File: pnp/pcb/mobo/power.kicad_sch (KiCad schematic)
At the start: 31 parts, among them J12 COMBO_POWER_JACK, U11 FDS4435BZ, U12 TPS54331, U13 AP1117-33, U6 Fuse_Holder_3568

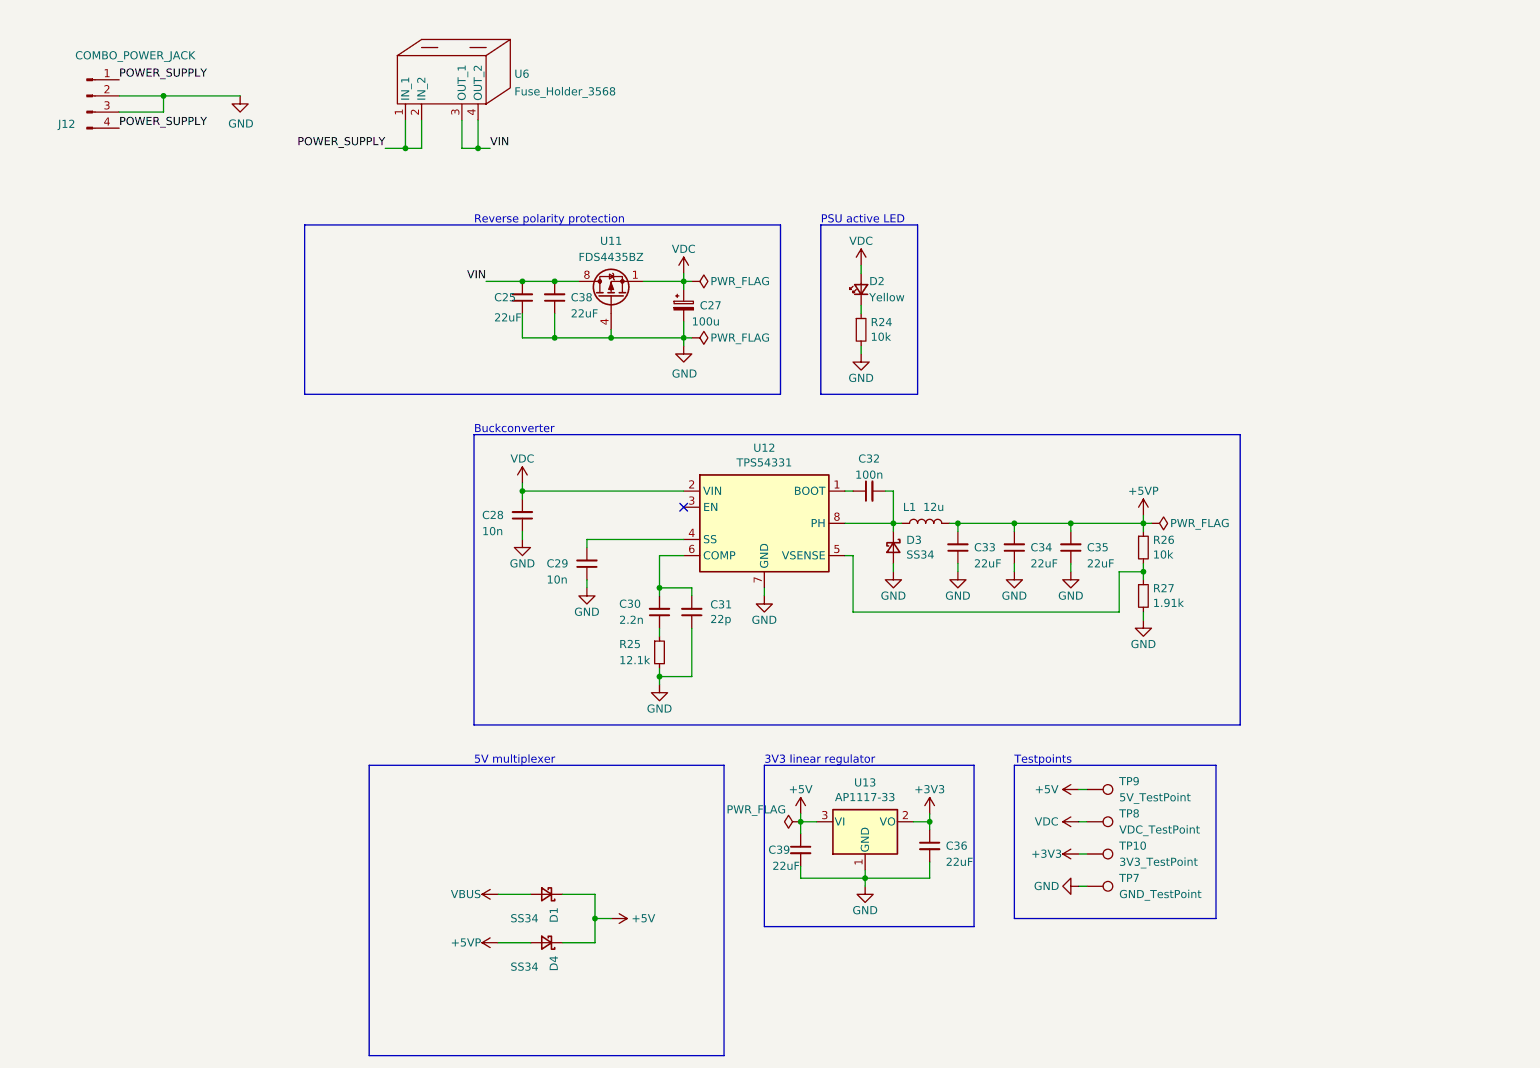
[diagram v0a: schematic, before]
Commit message: Mobo V4A Redesign
Some EMC improvements to schematics.
Reassigned MCU Pins for HW-PWM support.
Changes are still marked with text in the schematics.
Complete PCB Layout reworked
Status: Needs to be verified, and cleaned up a little, but DRC is running green.
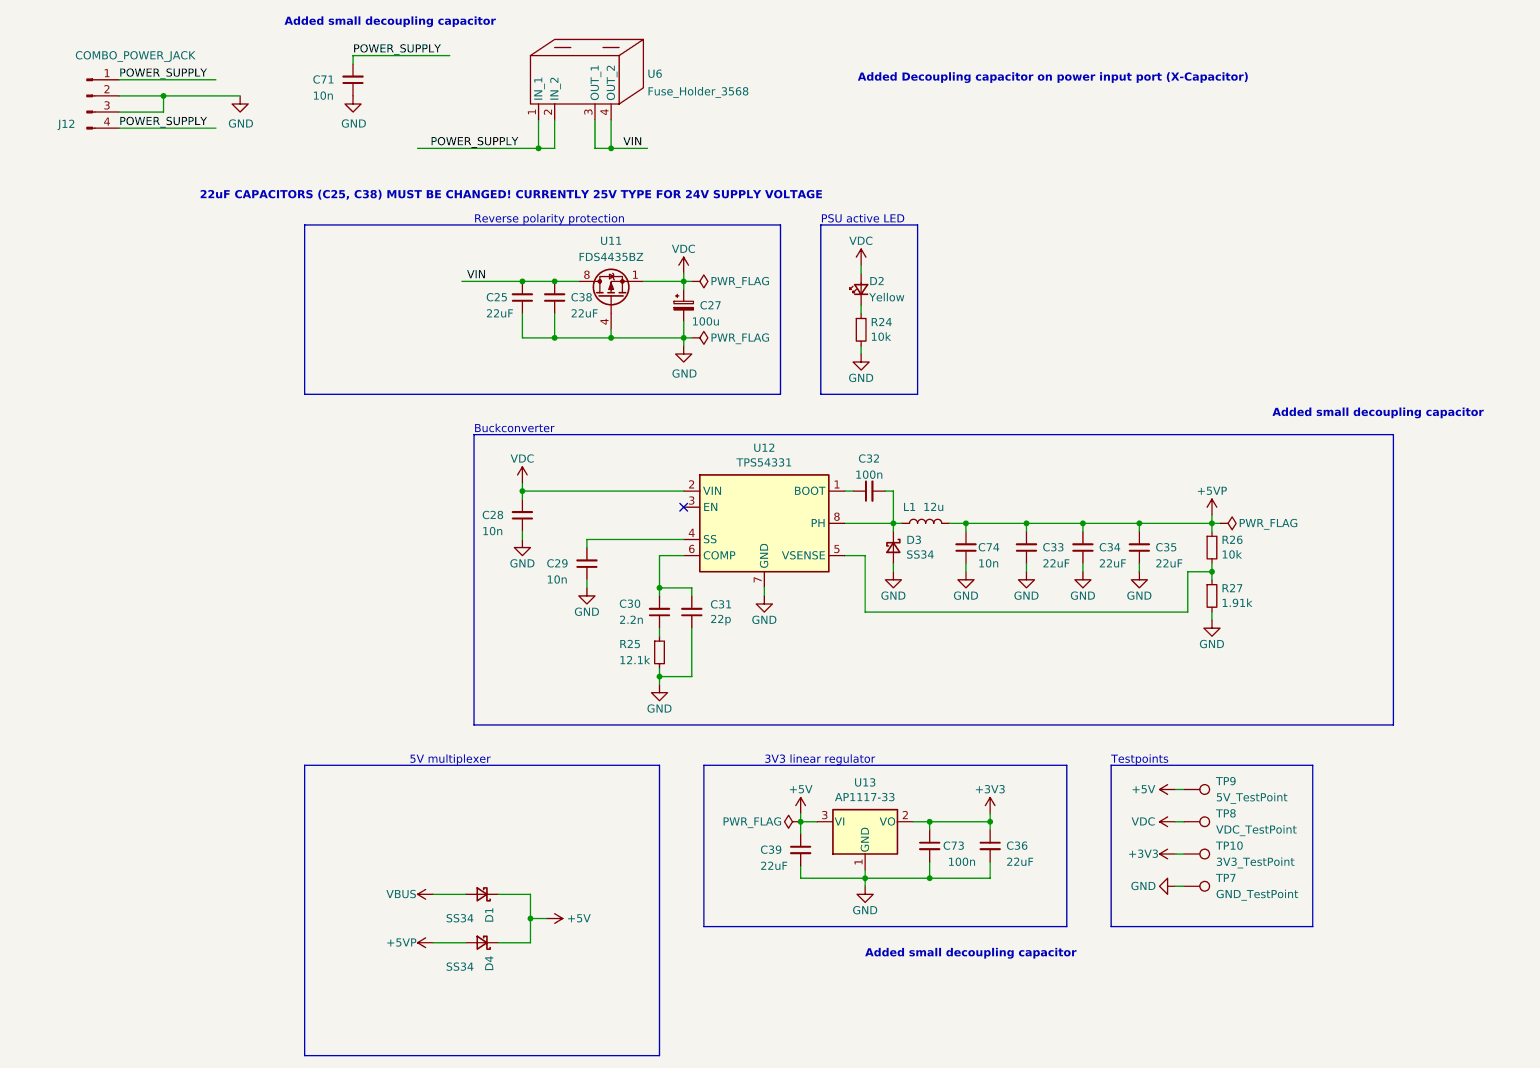
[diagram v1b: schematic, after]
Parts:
- added C71, C74: 10n, Capacitor_SMD:C_0805_2012Metric, symbol Device:C_Small
- added C73: 100n, Capacitor_SMD:C_0805_2012Metric, symbol Device:C_Small
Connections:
- net +3V3: now also C73.1
- net +5VP: now also C74.2
- net GND: now also C71.1, C73.2, C74.1
- net POWER_SUPPLY: now also C71.2
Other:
- note added: "22uF CAPACITORS (C25, C38) MUST BE CHANGED! CURRENTLY 25V TYPE FOR 24V SUPPLY VOLTAGE"
- note added: "Added Decoupling capacitor on power input port (X-Capacitor)"
- note added: "Added small decoupling capacitor"
- moved on the sheet: C33, C34, C35, C36, D1, D4, R26, R27, TP10, TP7, TP8, TP9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

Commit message: Redesign finished
Completed Board redesign and adding more EMC improvements.
Changed all the part numbers to have a Mouser orderable design (except the JST connectors)
All outputs generated
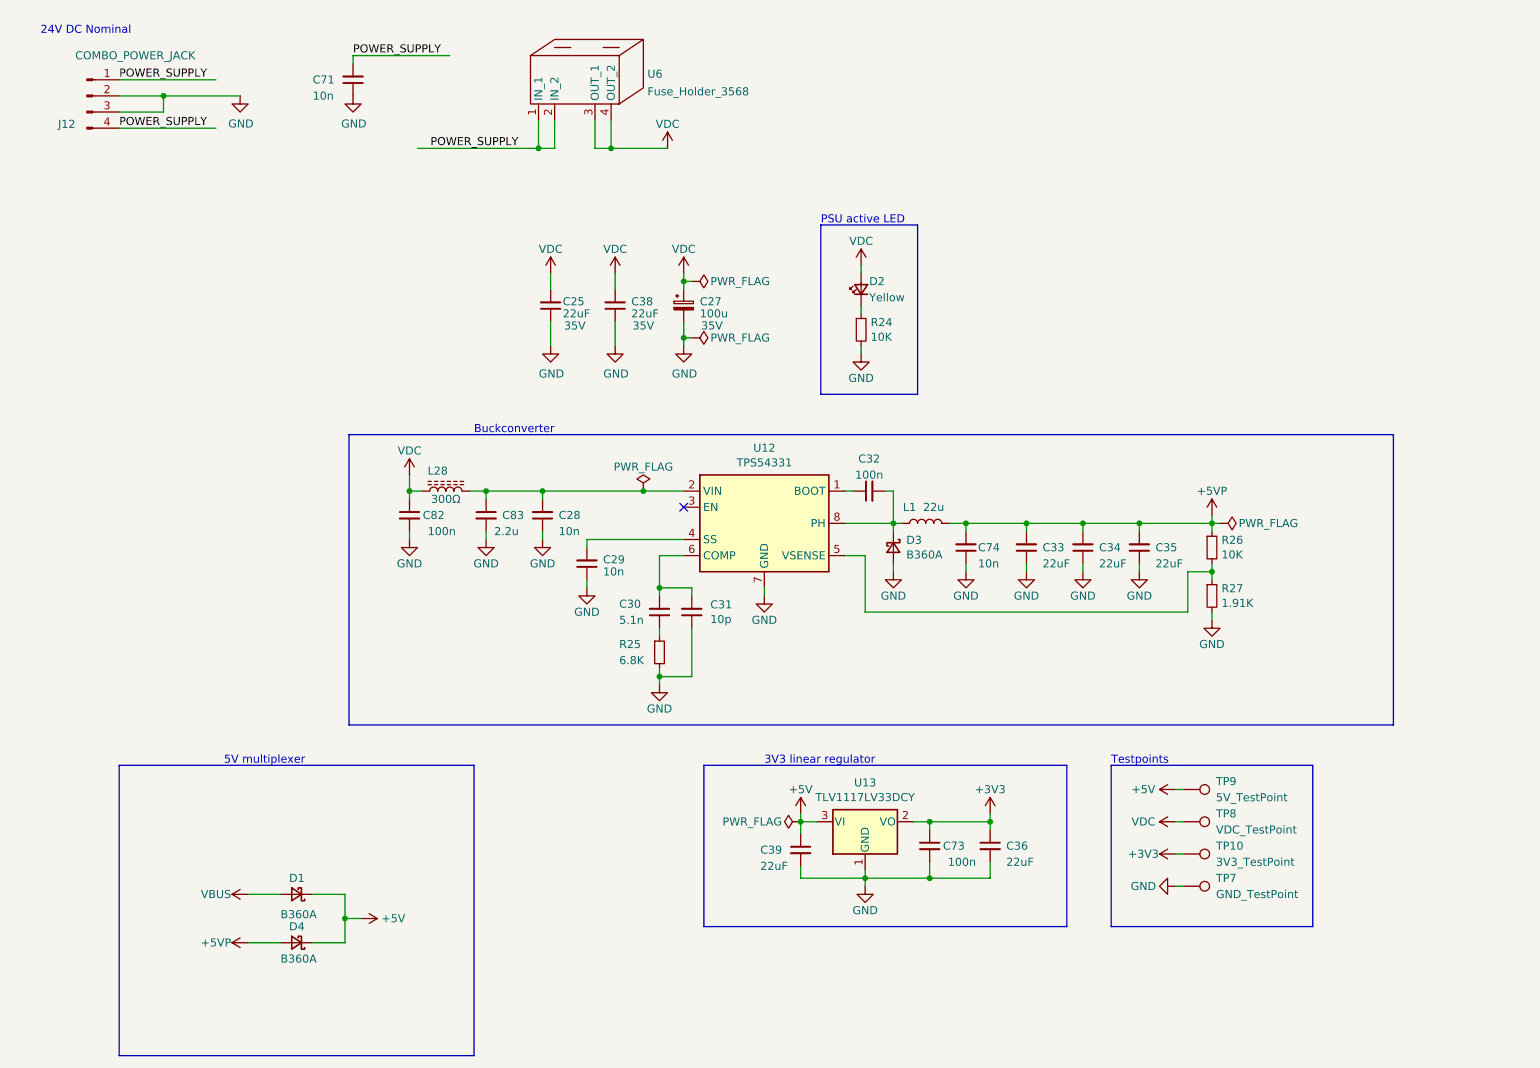
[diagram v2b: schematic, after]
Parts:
- removed U11: FDS4435BZ, Package_SO:SO-8_3.9x4.9mm_P1.27mm, symbol index:FDS4435BZ
- added C82: 100n, Capacitor_SMD:C_0805_2012Metric, symbol Device:C_Small
- added C83: 2.2u, Capacitor_SMD:C_0805_2012Metric, symbol Device:C_Small
- added L28: 300Ω, Inductor_SMD:L_0805_2012Metric, symbol Device:300Ω
- C25, C38: JLCPCB C45783 -> (none); LCSC C5674 -> (none); Mouser (none) -> 810-C2012X5R1V226MAC; Voltage (none) -> 35V
- C27: Digikey 493-2203-1-ND -> (none); JLCPCB C99837 -> (none); LCSC C3339 -> (none); Mouser 647-UWT1V101MCL1S -> 710-865080545012; Voltage (none) -> 35V
- C28, C29, C71, C74: JLCPCB C1710 -> (none); LCSC C1710 -> (none)
- C30: value 2.2n -> 5.1n; Digikey 1276-2993-1-ND -> (none); JLCPCB C28260 -> (none); LCSC C28260 -> (none); Mouser 187-CL21C222JBFNNNE -> 81-GRM2195C1H512JA1D
- C31: value 22p -> 10p; Digikey 311-1103-1-ND -> (none); JLCPCB C1804 -> (none); LCSC C123642 -> (none); Mouser 603-CC805JRNPO9BN220 -> 603-CC805JRNPO9BN100
- C32, C73: Digikey 1276-1180-1-ND -> (none); JLCPCB C49678 -> (none); LCSC C360619 -> (none); Mouser 581-08055C104K -> 710-885012207098
- C33, C34, C35: JLCPCB C45783 -> (none); LCSC C5674 -> (none); Mouser (none) -> 81-GRM21BR61E226ME4K
- C36, C39: Digikey 490-18663-1-ND -> (none); JLCPCB C15850 -> (none); LCSC C17024 -> (none); Mouser 81-GRM21BR61H106KE3L -> 81-GRM21BR61E226ME4K
- D1, D3, D4: value SS34 -> B360A; Digikey 641-2115-1-ND -> (none); JLCPCB C8678 -> (none); LCSC C266553 -> (none); Mouser 821-SS34LRVG -> 625-B360A-E3/61T
- D2: JLCPCB C2296 -> (none); LCSC C779458 -> (none)
- J12: Mouser (none) -> 710-694106301002
- L1: value 12u -> 22u; footprint Inductor_SMD:L_Coilcraft_XAL60xx_6.36x6.56mm -> Inductor_SMD:L_Bourns_SRP7028A_7.3x6.6mm; Digikey ASPI-6045S-120M-TCT-ND -> (none); LCSC C168077 -> (none); Mouser 815-ASPI-6045S-120MT -> 652-SRP7028C-220M
- R24: value 10k -> 10K; Digikey RMCF0805FT10K0CT-ND -> (none); JLCPCB C17414 -> (none); LCSC C115295 -> (none); Mouser 71-CRCW080510K0FKEAC -> 603-RC0805FR-1010KL
- R25: value 12.1k -> 6.8K; Digikey 541-12.1KCCT-ND -> (none); JLCPCB C17431 -> (none); LCSC C139928 -> (none); Mouser 71-CRCW0805-12.1K-E3 -> 603-RT0603FRE076K8L
- R26: value 10k -> 10K; Digikey RMCF0805FT10K0CT-ND -> (none); JLCPCB C17414 -> (none); LCSC C115295 -> (none); Mouser 71-CRCW080510K0FKEAC -> 603-RC0805FR-1010KL; Notes 1% -> (none)
- R27: value 1.91k -> 1.91K; Digikey 541-1.91KCCT-ND -> (none); JLCPCB C17401 -> (none); LCSC C17401 -> (none)
- TP10, TP7, TP8, TP9: Mouser (none) -> -
- U12: JLCPCB C9865 -> (none); LCSC C9865 -> (none)
- U13: value AP1117-33 -> TLV1117LV33DCY; Digikey ZLDO1117G33DICT-ND -> 296-35976-1-ND; JLCPCB C108785 -> (none); LCSC C108785 -> (none); Mouser 522-ZLDO1117G33TA -> 595-TLV1117LV33DCYT
- U6: Mouser (none) -> 534-3568
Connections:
- net VIN is gone; now on net VDC: C25.2, C38.2, U6.3 (OUT_1), U6.4 (OUT_2)
- net GND: now also C82.2, C83.2
- net VDC: now also C82.1, L28.1; no longer C28.2, U12.2 (VIN)
- new net: C28.2, C83.1, L28.2, U12.2 (VIN)
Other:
- note added: "24V DC Nominal"
- note removed: "22uF CAPACITORS (C25, C38) MUST BE CHANGED! CURRENTLY 25V TYPE FOR 24V SUPPLY VOLTAGE"
- note removed: "Added Decoupling capacitor on power input port (X-Capacitor)"
- note removed: "Added small decoupling capacitor"
- note removed: "Reverse polarity protection"
- company: Opulo -> Opulo.io
- moved on the sheet: C25, C28, D1, D4
